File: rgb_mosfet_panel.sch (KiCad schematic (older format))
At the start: 88 parts, among them J1 USB_B_Micro, Q1 DMG2302U, Q2 DMG2302U, Q3 DMG2302U, Q4 DMG2302U, Q5 DMG2302U, U1 TC2014-3.3VxCTTR, U2 MCP1640CH, U3 ATtiny13A-SSU, X1 SXO-53C3A071

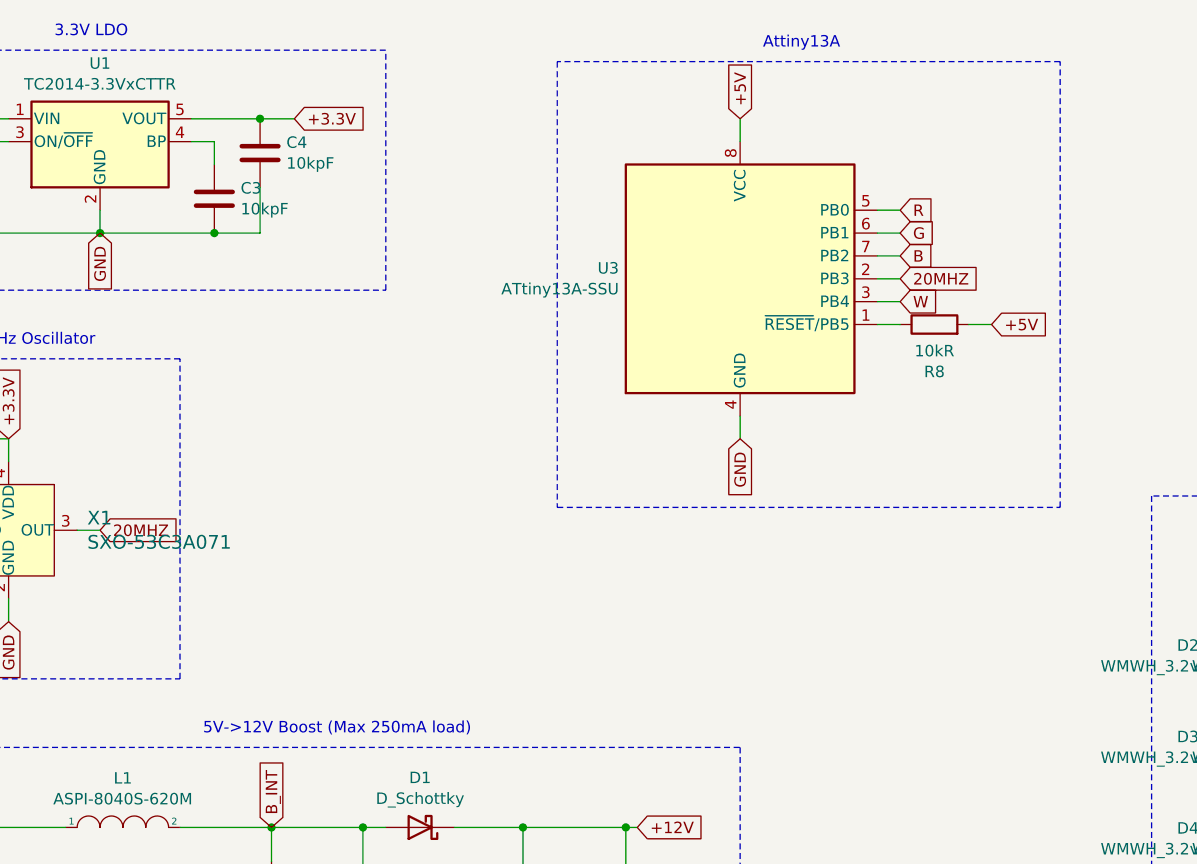
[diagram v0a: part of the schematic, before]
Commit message: Add ISP header
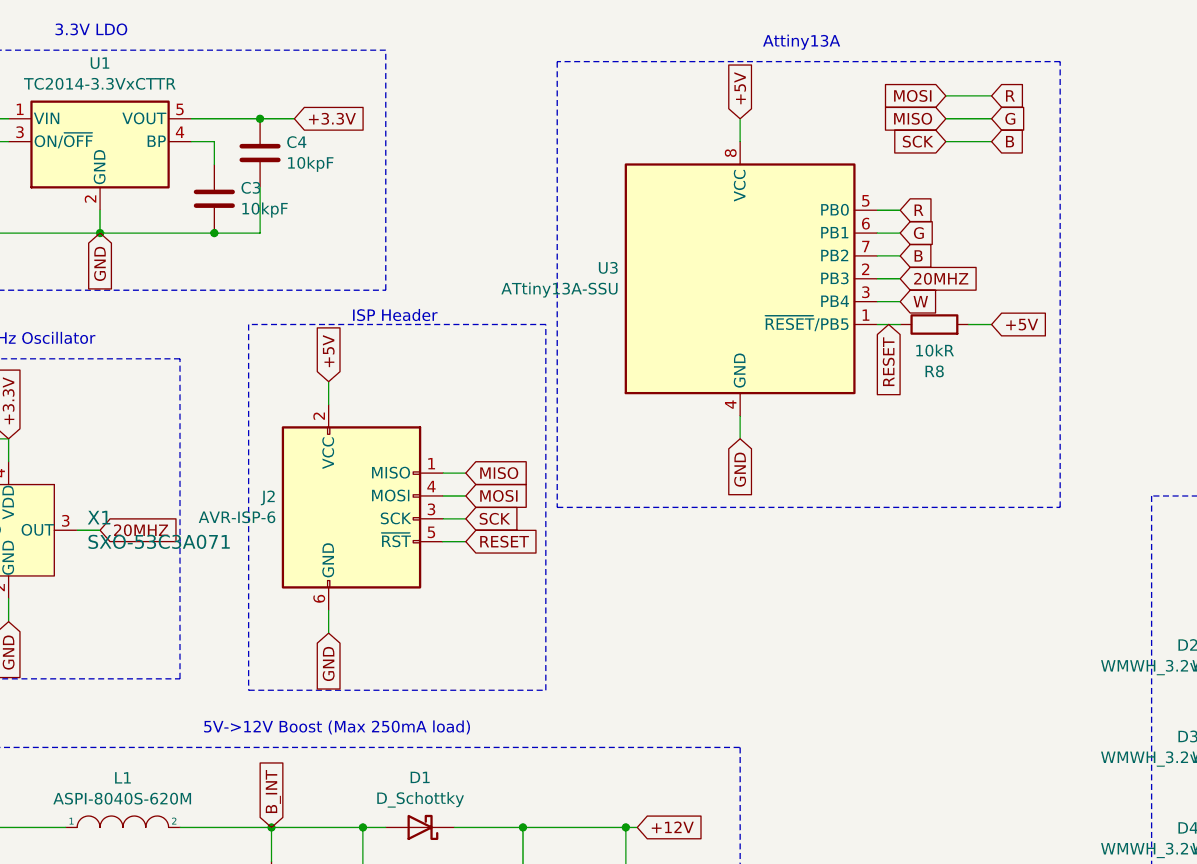
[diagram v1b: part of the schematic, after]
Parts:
- added J2: AVR-ISP-6, Connector_PinHeader_2.54mm:PinHeader_2x03_P2.54mm_Vertical_SMD, symbol Connector:AVR-ISP-6
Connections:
- net +5V: now also J2.2 (VCC)
- net B: now also J2.3 (SCK)
- net G: now also J2.1 (MISO)
- net GND: now also J2.6 (GND)
- net RESET: now reaches R8.1, U3.1 (~RESET~/PB5)
- net RESET: now also J2.5 (~RST)
- net R renamed MOSI
- net MOSI: now also J2.4 (MOSI)
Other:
- note added: "ISP Header"
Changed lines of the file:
@@
 $EndDescr
-$Comp
-L MCU_Microchip_ATtiny:ATtiny13A-SSU U3
-U 1 1 600AD815
-P 4550 1600
-F 0 "U3" H 4020 1646 50  0000 R CNN
-F 1 "ATtiny13A-SSU" H 4020 1555 50  0000 R CNN
-F 2 "Package_SO:SOIC-8_3.9x4.9mm_P1.27mm" H 4550 1600 50  0001 C CIN
-F 3 "http://ww1.microchip.com/downloads/en/DeviceDoc/doc8126.pdf" H 4550 1600 50  0001 C CNN
-	1    4550 1600
-	1    0    0    -1
-$EndComp
 $Comp
 L Device:LED D14
@@
 	1    0    0    -1
 $EndComp
+$Comp
+L Connector:AVR-ISP-6 J2
+U 1 1 600F0641
+P 2850 2650
+F 0 "J2" H 2521 2746 50  0000 R CNN
+F 1 "AVR-ISP-6" H 2521 2655 50  0000 R CNN
+F 2 "Connector_PinHeader_2.54mm:PinHeader_2x03_P2.54mm_Vertical_SMD" V 2600 2700 50  0001 C CNN
+F 3 " ~" H 1575 2100 50  0001 C CNN
+	1    2850 2650
+	1    0    0    -1
+$EndComp
+Text GLabel 2750 2050 1    50   Input ~ 0
++5V
+Wire Wire Line
+	2750 2050 2750 2150
+Text GLabel 2750 3150 3    50   Input ~ 0
+GND
+Wire Wire Line
+	2750 3050 2750 3150
+Text GLabel 5200 1800 3    50   Input ~ 0
+RESET
+Text GLabel 3350 2750 2    50   Input ~ 0
+RESET
+Wire Wire Line
+	3350 2750 3250 2750
+Text GLabel 3350 2450 2    50   Input ~ 0
+MISO
+Text GLabel 3350 2550 2    50   Input ~ 0
+MOSI
+Text GLabel 3350 2650 2    50   Input ~ 0
+SCK
+Wire Wire Line
+	3250 2450 3350 2450
+Wire Wire Line
+	3250 2550 3350 2550
+Wire Wire Line
+	3250 2650 3350 2650
+Text GLabel 5650 800  2    50   Input ~ 0
+R
+Text GLabel 5650 900  2    50   Input ~ 0
+G
+Text GLabel 5650 1000 2    50   Input ~ 0
+B
+Text GLabel 5450 1000 0    50   Input ~ 0
+SCK
+Text GLabel 5450 800  0    50   Input ~ 0
+MOSI
+Text GLabel 5450 900  0    50   Input ~ 0
+MISO
+$Comp
+L MCU_Microchip_ATtiny:ATtiny13A-SSU U3
+U 1 1 600AD815
+P 4550 1600
+F 0 "U3" H 4020 1646 50  0000 R CNN
+F 1 "ATtiny13A-SSU" H 4020 1555 50  0000 R CNN
+F 2 "Package_SO:SOIC-8_3.9x4.9mm_P1.27mm" H 4550 1600 50  0001 C CIN
+F 3 "http://ww1.microchip.com/downloads/en/DeviceDoc/doc8126.pdf" H 4550 1600 50  0001 C CNN
+	1    4550 1600
+	1    0    0    -1
+$EndComp
+Wire Wire Line
+	5450 1000 5650 1000
+Wire Wire Line
+	5450 800  5650 800
+Wire Wire Line
+	5450 900  5650 900
+Wire Notes Line
+	2400 1800 2400 3400
+Wire Notes Line
+	2400 3400 3700 3400
+Wire Notes Line
+	3700 3400 3700 1800
+Wire Notes Line
+	3700 1800 2400 1800
+Text Notes 2850 1800 0    50   ~ 0
+ISP Header
 $EndSCHEMATC

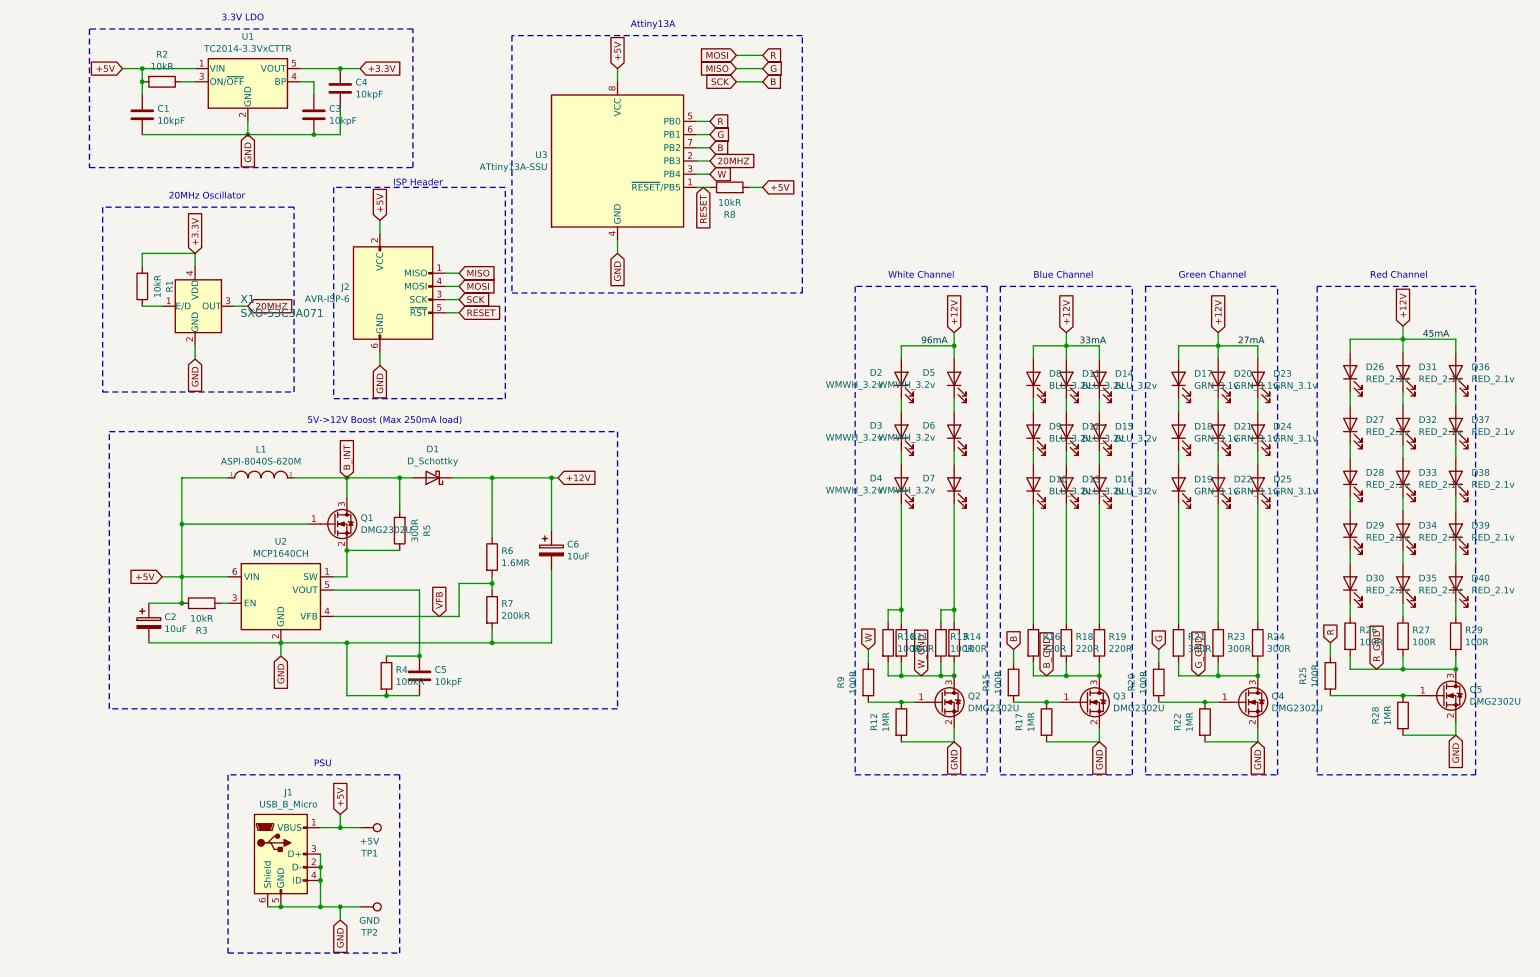
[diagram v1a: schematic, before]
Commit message: Update to use MIC2250
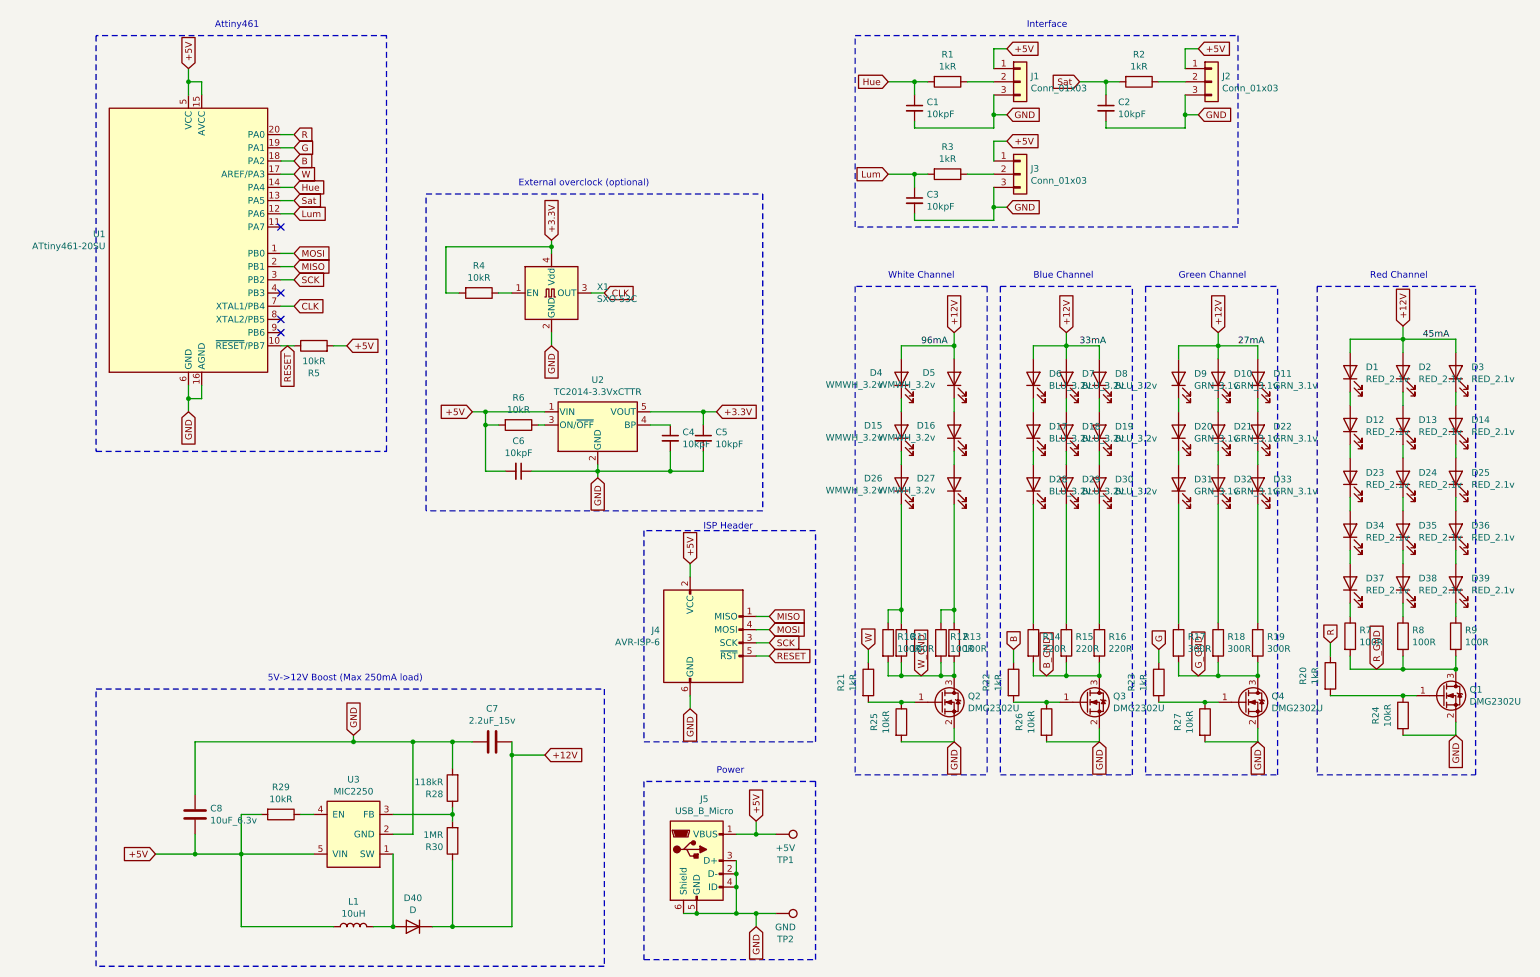
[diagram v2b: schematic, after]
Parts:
- removed C1, C3, C4, C5: 10kpF, Capacitor_SMD:C_0603_1608Metric, symbol Device:C
- removed C2, C6: 10uF, Capacitor_THT:CP_Radial_D4.0mm_P1.50mm, symbol Device:CP
- removed D1: D_Schottky, Diode_SMD:D_SOD-123, symbol Device:D_Schottky
- removed L1: ASPI-8040S-620M, Inductor_SMD:L_Taiyo-Yuden_NR-80xx, symbol pspice:INDUCTOR
- removed Q1: DMG2302U, Package_TO_SOT_SMD:SOT-23, symbol Transistor_FET:DMG2302U
- removed R5: 300R, Resistor_SMD:R_0805_2012Metric, symbol Device:R
- removed R7: 200kR, Resistor_SMD:R_0805_2012Metric, symbol Device:R
- removed U1: TC2014-3.3VxCTTR, Package_TO_SOT_SMD:SOT-23-5, symbol Regulator_Linear:TC2014-3.3VxCTTR
- removed U2: MCP1640CH, Package_TO_SOT_SMD:SOT-23-6, symbol Regulator_Switching:MCP1640CH
- removed U3: ATtiny13A-SSU, Package_SO:SOIC-8_3.9x4.9mm_P1.27mm, symbol MCU_Microchip_ATtiny:ATtiny13A-SSU
- removed X1: SXO-53C3A071, Oscillator:Oscillator_SMD_TXC_7C-4Pin_5.0x3.2mm, symbol dk_Oscillators:XLH736022_579200I
- added C1, C2, C3, C4, C5, C6: 10kpF, Capacitor_SMD:C_0603_1608Metric, symbol Device:C_Small
- added C7: 2.2uF_15v, Capacitor_SMD:C_0603_1608Metric, symbol Device:C
- added C8: 10uF_6.3v, Capacitor_SMD:C_0603_1608Metric, symbol Device:C
- added D40: D, Diode_SMD:D_SMA, symbol Device:D
- added J1, J2, J3: Conn_01x03, Jumper:SolderJumper-3_P1.3mm_Open_Pad1.0x1.5mm_NumberLabels, symbol Connector_Generic:Conn_01x03
- added L1: 10uH, Inductor_SMD:L_Taiyo-Yuden_NR-50xx, symbol Device:L
- added R28: 118kR, Resistor_SMD:R_0805_2012Metric, symbol Device:R
- added R29: 10kR, Resistor_SMD:R_0805_2012Metric, symbol Device:R
- added R30: 1MR, Resistor_SMD:R_0805_2012Metric, symbol Device:R
- added U1: ATtiny461-20SU, Package_SO:TSSOP-20_4.4x6.5mm_P0.65mm, symbol MCU_Microchip_ATtiny:ATtiny461A-XU
- added U2: TC2014-3.3VxCTTR, Package_TO_SOT_SMD:SOT-23-5, symbol Regulator_Linear:TC2014-3.3VxCTTR
- added U3: MIC2250, Package_TO_SOT_SMD:TSOT-23-5, symbol WM_lib:MIC2250
- added X1: SXO-53C, Oscillator:Oscillator_SMD_TXC_7C-4Pin_5.0x3.2mm, symbol Oscillator:TXC-7C
- R1, R2, R3: value 10kR -> 1kR
- R20: renamed from R25; value 100R -> 1kR
- R21: renamed from R9; value 100R -> 1kR
- R22: renamed from R15; value 100R -> 1kR
- R23: renamed from R20; value 100R -> 1kR
- R24: renamed from R28; value 1MR -> 10kR
- R25: renamed from R12; value 1MR -> 10kR
- R26: renamed from R17; value 1MR -> 10kR
- R27: renamed from R22; value 1MR -> 10kR
- R4: value 100kR -> 10kR
- R6: value 1.6MR -> 10kR
- renumbered D26 to D1, D20 to D10, D23 to D11, D27 to D12, D32 to D13, D37 to D14, D3 to D15, D6 to D16, D9 to D17, D12 to D18, D15 to D19, D31 to D2, D18 to D20, D24 to D22, D28 to D23, D33 to D24, D38 to D25, D4 to D26, D7 to D27, D10 to D28, D13 to D29, D36 to D3, D16 to D30, D19 to D31, D22 to D32, D25 to D33, D29 to D34, D34 to D35, D39 to D36, D30 to D37, D35 to D38, D40 to D39, D2 to D4, D8 to D6, D11 to D7, D14 to D8, D17 to D9, J2 to J4, J1 to J5, Q5 to Q1, R13 to R12, R14 to R13, R16 to R14, R18 to R15, R19 to R16, R21 to R17, R23 to R18, R24 to R19, R8 to R5, R26 to R7, R27 to R8, R29 to R9
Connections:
- net VFB is gone; now on net +5V: R6.2
- net +12V: now also C7.2, D40.1 (K), R30.1; no longer R6.1
- net +3.3V: now also R4.2, C5.1, U2.5 (VOUT), X1.4 (Vdd); no longer R1.2
- net +5V: now also C6.2, C8.2, J1.1 (Pin_1), J2.1 (Pin_1), J3.1 (Pin_1), L1.1, R29.2, U1.15 (AVCC), U1.5 (VCC), U2.1 (VIN), U3.5 (VIN); no longer R2.2, R3.1
- net B: now also U1.18 (PA2); no longer J4.3 (SCK)
- net G: now also U1.19 (PA1); no longer J4.1 (MISO)
- net GND: now also C1.2, C2.2, C3.2, C4.2, C5.2, C6.1, C7.1, C8.1, J1.3 (Pin_3), J2.3 (Pin_3), J3.3 (Pin_3), R28.2, U1.16 (AGND), U1.6 (GND), U2.2 (GND), U3.2 (GND), X1.2 (GND); no longer R4.2
- net MOSI: now also U1.1 (PB0); no longer R20.1
- net RESET: now also U1.10 (~RESET~/PB7)
- net W: now also U1.17 (AREF/PA3)
- net at R2.1: now also J2.2 (Pin_2)
- net at R1.1: now also J1.2 (Pin_2)
- net Lum: now reaches R3.2
- net Lum: now also C3.1, U1.12 (PA6)
- net at R4.1: now also X1.1 (EN)
- new net: D40.2 (A), L1.2, U3.1 (SW)
- new net: R28.1, R30.2, U3.3 (FB)
- new net: R29.1, U3.4 (EN)
- new net: R6.1, U2.3 (ON/~OFF~)
- new net: C4.1, U2.4 (BP)
- new net: J3.2 (Pin_2), R3.1
- new net CLK: U1.7 (XTAL1/PB4), X1.3 (OUT)
- new net Hue: C1.1, R1.2, U1.14 (PA4)
- new net MISO: J4.1 (MISO), U1.2 (PB1)
- new net R: R20.1, U1.20 (PA0)
- new net SCK: J4.3 (SCK), U1.3 (PB2)
- new net Sat: C2.1, R2.2, U1.13 (PA5)
- no-connect marks 0 -> 4
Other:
- note added: "Attiny461"
- note added: "External overclock (optional)"
- note added: "Interface"
- note added: "Power"
- note removed: "20MHz Oscillator"
- note removed: "3.3V LDO"
- note removed: "Attiny13A"
- note removed: "PSU"
- moved on the sheet: J4, J5, R5, TP1, TP2
